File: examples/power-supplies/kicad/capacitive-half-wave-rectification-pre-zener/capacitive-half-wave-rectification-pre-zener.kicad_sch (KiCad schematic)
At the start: 11 parts

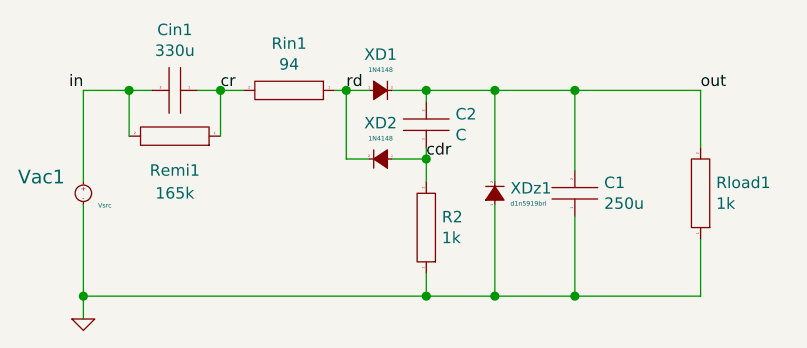
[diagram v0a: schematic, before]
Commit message: kicad fix
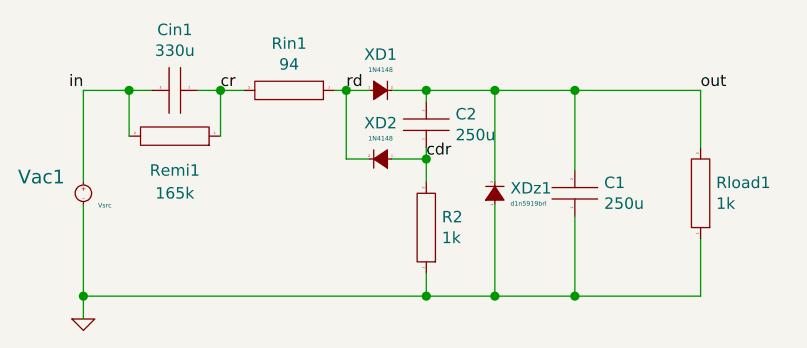
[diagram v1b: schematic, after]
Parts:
- C2: value C -> 250u
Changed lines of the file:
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@@
       (effects (font (size 1.27 1.27)) (justify right))
     )
-    (property "Value" "C" (id 1) (at 148.0312 78.613 0)
+    (property "Value" "250u" (id 1) (at 148.0312 78.613 0)
       (effects (font (size 1.27 1.27)) (justify right))
     )
@@
     )
     (path "/00000000-0000-0000-0000-00006099f76f"
-      (reference "C2") (unit 1) (value "C") (footprint "")
+      (reference "C2") (unit 1) (value "250u") (footprint "")
     )
     (path "/00000000-0000-0000-0000-00006099bee2"
